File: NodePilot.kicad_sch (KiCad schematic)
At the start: 44 parts, among them K1 SRD-05VDC-SL-C, Q1 2N3904, Q2 2N2222, Q4 2N3904, T1 1:1 600R, T2 1:1 600R, U1 PC817, U2 PC817, U3 B0505S-1WR2, U4 LM358_DFN

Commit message: footprints resistors caps and diode
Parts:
- C1, C2, C3, C4, C5, C6, C8: footprint (none) -> Capacitor_THT:CP_Radial_D5.0mm_P2.50mm
- C10, C11, C7, C9: footprint (none) -> C_Disc_D5.0mm_W2.5mm_P2.50mm
- R1, R10, R11, R12, R13, R14, R16, R17, R18, R19, R2, R20, R3, R4, R5, R6, R7, R8, R9: footprint (none) -> R_Axial_DIN0204_L3.6mm_D1.6mm_P5.08mm_Horizontal
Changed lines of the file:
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@@
 			)
 		)
-		(property "Footprint" ""
+		(property "Footprint" "C_Disc_D5.0mm_W2.5mm_P2.50mm"
 			(at 95.25 88.9 0)
 			(hide yes)
@@
 			)
 		)
-		(property "Footprint" ""
+		(property "Footprint" "R_Axial_DIN0204_L3.6mm_D1.6mm_P5.08mm_Horizontal"
 			(at 49.276 71.374 90)
 			(hide yes)
@@
 			)
 		)
-		(property "Footprint" ""
+		(property "Footprint" "R_Axial_DIN0204_L3.6mm_D1.6mm_P5.08mm_Horizontal"
 			(at 122.936 48.514 90)
 			(hide yes)
@@
 			)
 		)
-		(property "Footprint" ""
+		(property "Footprint" "Capacitor_THT:CP_Radial_D5.0mm_P2.50mm"
 			(at 114.3 110.1852 0)
 			(hide yes)
@@
 			)
 		)
-		(property "Footprint" ""
+		(property "Footprint" "R_Axial_DIN0204_L3.6mm_D1.6mm_P5.08mm_Horizontal"
 			(at 106.934 70.104 90)
 			(hide yes)
@@
 			)
 		)
-		(property "Footprint" ""
+		(property "Footprint" "C_Disc_D5.0mm_W2.5mm_P2.50mm"
 			(at 110.49 119.38 0)
 			(hide yes)
@@
 			)
 		)
-		(property "Footprint" ""
+		(property "Footprint" "Capacitor_THT:CP_Radial_D5.0mm_P2.50mm"
 			(at 114.3 101.9048 0)
 			(hide yes)
@@
 			)
 		)
-		(property "Footprint" ""
+		(property "Footprint" "C_Disc_D5.0mm_W2.5mm_P2.50mm"
 			(at 184.15 92.71 0)
 			(hide yes)
@@
 			)
 		)
-		(property "Footprint" ""
+		(property "Footprint" "R_Axial_DIN0204_L3.6mm_D1.6mm_P5.08mm_Horizontal"
 			(at 211.074 82.804 90)
 			(hide yes)
@@
 			)
 		)
-		(property "Footprint" ""
+		(property "Footprint" "R_Axial_DIN0204_L3.6mm_D1.6mm_P5.08mm_Horizontal"
 			(at 86.106 180.594 90)
 			(hide yes)
@@
 			)
 		)
-		(property "Footprint" ""
+		(property "Footprint" "Capacitor_THT:CP_Radial_D5.0mm_P2.50mm"
 			(at 128.27 23.1648 0)
 			(hide yes)
@@
 			)
 		)
-		(property "Footprint" ""
+		(property "Footprint" "R_Axial_DIN0204_L3.6mm_D1.6mm_P5.08mm_Horizontal"
 			(at 159.766 91.694 90)
 			(hide yes)
@@
 			)
 		)
-		(property "Footprint" ""
+		(property "Footprint" "R_Axial_DIN0204_L3.6mm_D1.6mm_P5.08mm_Horizontal"
 			(at 95.504 53.594 90)
 			(hide yes)
@@
 			)
 		)
-		(property "Footprint" ""
+		(property "Footprint" "Capacitor_THT:CP_Radial_D5.0mm_P2.50mm"
 			(at 106.68 53.6448 0)
 			(hide yes)
@@
 			)
 		)
-		(property "Footprint" ""
+		(property "Footprint" "R_Axial_DIN0204_L3.6mm_D1.6mm_P5.08mm_Horizontal"
 			(at 70.866 85.344 90)
 			(hide yes)
@@
 			)
 		)
-		(property "Footprint" ""
+		(property "Footprint" "Capacitor_THT:CP_Radial_D5.0mm_P2.50mm"
 			(at 187.96 28.2448 0)
 			(hide yes)
@@
 			)
 		)
-		(property "Footprint" ""
+		(property "Footprint" "R_Axial_DIN0204_L3.6mm_D1.6mm_P5.08mm_Horizontal"
 			(at 92.964 129.794 90)
 			(hide yes)
@@
 			)
 		)
-		(property "Footprint" ""
+		(property "Footprint" "R_Axial_DIN0204_L3.6mm_D1.6mm_P5.08mm_Horizontal"
 			(at 184.404 113.284 90)
 			(hide yes)
@@
 			)
 		)
-		(property "Footprint" ""
+		(property "Footprint" "R_Axial_DIN0204_L3.6mm_D1.6mm_P5.08mm_Horizontal"
 			(at 152.146 29.464 90)
 			(hide yes)
@@
 			)
 		)
-		(property "Footprint" ""
+		(property "Footprint" "R_Axial_DIN0204_L3.6mm_D1.6mm_P5.08mm_Horizontal"
 			(at 86.106 165.354 90)
 			(hide yes)
@@
 			)
 		)
-		(property "Footprint" ""
+		(property "Footprint" "R_Axial_DIN0204_L3.6mm_D1.6mm_P5.08mm_Horizontal"
 			(at 196.596 92.964 90)
 			(hide yes)
@@
 			)
 		)
-		(property "Footprint" ""
+		(property "Footprint" "R_Axial_DIN0204_L3.6mm_D1.6mm_P5.08mm_Horizontal"
 			(at 78.486 176.784 90)
 			(hide yes)
@@
 			)
 		)
-		(property "Footprint" ""
+		(property "Footprint" "Capacitor_THT:CP_Radial_D5.0mm_P2.50mm"
 			(at 175.26 57.4548 0)
 			(hide yes)
@@
 			)
 		)
-		(property "Footprint" ""
+		(property "Footprint" "R_Axial_DIN0204_L3.6mm_D1.6mm_P5.08mm_Horizontal"
 			(at 196.596 76.454 90)
 			(hide yes)
@@
 			)
 		)
-		(property "Footprint" ""
+		(property "Footprint" "R_Axial_DIN0204_L3.6mm_D1.6mm_P5.08mm_Horizontal"
 			(at 49.784 129.794 90)
 			(hide yes)
@@
 			)
 		)
-		(property "Footprint" ""
+		(property "Footprint" "R_Axial_DIN0204_L3.6mm_D1.6mm_P5.08mm_Horizontal"
 			(at 157.734 146.304 90)
 			(hide yes)
@@
 			)
 		)
-		(property "Footprint" ""
+		(property "Footprint" "C_Disc_D5.0mm_W2.5mm_P2.50mm"
 			(at 58.42 133.35 0)
 			(hide yes)
@@
 			)
 		)
-		(property "Footprint" ""
+		(property "Footprint" "Capacitor_THT:CP_Radial_D5.0mm_P2.50mm"
 			(at 104.4448 85.09 0)
 			(hide yes)
@@
 			)
 		)
-		(property "Footprint" ""
+		(property "Footprint" "R_Axial_DIN0204_L3.6mm_D1.6mm_P5.08mm_Horizontal"
 			(at 71.374 169.164 90)
 			(hide yes)
@@
 			)
 		)
-		(property "Footprint" ""
+		(property "Footprint" "R_Axial_DIN0204_L3.6mm_D1.6mm_P5.08mm_Horizontal"
 			(at 127.254 139.954 90)
 			(hide yes)

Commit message: footprints t1
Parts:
- JP1: footprint (none) -> Connector:JWT_A3963_1x02_P3.96mm_Vertical
- U3: symbol B0505s:B0505S-1WR2 -> B0505S-1WR2:B0505S-1WR2
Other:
- moved on the sheet: U3
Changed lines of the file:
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@@
 			)
 		)
-		(property "Footprint" ""
+		(property "Footprint" "Connector:JWT_A3963_1x02_P3.96mm_Vertical"
 			(at 195.58 64.77 0)
 			(hide yes)
@@
 	)
 	(symbol
-		(lib_id "B0505s:B0505S-1WR2")
+		(lib_id "B0505S-1WR2:B0505S-1WR2")
 		(at 115.57 102.87 0)
 		(mirror x)

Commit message: footprints t2
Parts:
- C10, C11, C7, C9: footprint C_Disc_D5.0mm_W2.5mm_P2.50mm -> Capacitor_THT:C_Disc_D5.0mm_W2.5mm_P2.50mm
- R1, R10, R11, R12, R13, R14, R16, R17, R18, R19, R2, R20, R3, R4, R5, R6, R7, R8, R9: footprint R_Axial_DIN0204_L3.6mm_D1.6mm_P5.08mm_Horizontal -> Resistor_THT:R_Axial_DIN0204_L3.6mm_D1.6mm_P5.08mm_Horizontal
- RV1, RV2: footprint (none) -> Potentiometer_THT:Potentiometer_Bourns_3386W_Horizontal
- U3: footprint B0505S-1WR2_MNS -> B0505S-WR1:B0505S-1WR2_MNS
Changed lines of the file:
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@@
 			)
 		)
-		(property "Footprint" "C_Disc_D5.0mm_W2.5mm_P2.50mm"
+		(property "Footprint" "Capacitor_THT:C_Disc_D5.0mm_W2.5mm_P2.50mm"
 			(at 95.25 88.9 0)
 			(hide yes)
@@
 			)
 		)
-		(property "Footprint" "R_Axial_DIN0204_L3.6mm_D1.6mm_P5.08mm_Horizontal"
+		(property "Footprint" "Resistor_THT:R_Axial_DIN0204_L3.6mm_D1.6mm_P5.08mm_Horizontal"
 			(at 49.276 71.374 90)
 			(hide yes)
@@
 			)
 		)
-		(property "Footprint" "R_Axial_DIN0204_L3.6mm_D1.6mm_P5.08mm_Horizontal"
+		(property "Footprint" "Resistor_THT:R_Axial_DIN0204_L3.6mm_D1.6mm_P5.08mm_Horizontal"
 			(at 122.936 48.514 90)
 			(hide yes)
@@
 			)
 		)
-		(property "Footprint" "R_Axial_DIN0204_L3.6mm_D1.6mm_P5.08mm_Horizontal"
+		(property "Footprint" "Resistor_THT:R_Axial_DIN0204_L3.6mm_D1.6mm_P5.08mm_Horizontal"
 			(at 106.934 70.104 90)
 			(hide yes)
@@
 			)
 		)
-		(property "Footprint" "C_Disc_D5.0mm_W2.5mm_P2.50mm"
+		(property "Footprint" "Capacitor_THT:C_Disc_D5.0mm_W2.5mm_P2.50mm"
 			(at 110.49 119.38 0)
 			(hide yes)
@@
 			)
 		)
-		(property "Footprint" "C_Disc_D5.0mm_W2.5mm_P2.50mm"
+		(property "Footprint" "Capacitor_THT:C_Disc_D5.0mm_W2.5mm_P2.50mm"
 			(at 184.15 92.71 0)
 			(hide yes)
@@
 			)
 		)
-		(property "Footprint" "R_Axial_DIN0204_L3.6mm_D1.6mm_P5.08mm_Horizontal"
+		(property "Footprint" "Resistor_THT:R_Axial_DIN0204_L3.6mm_D1.6mm_P5.08mm_Horizontal"
 			(at 211.074 82.804 90)
 			(hide yes)
@@
 			)
 		)
-		(property "Footprint" "R_Axial_DIN0204_L3.6mm_D1.6mm_P5.08mm_Horizontal"
+		(property "Footprint" "Resistor_THT:R_Axial_DIN0204_L3.6mm_D1.6mm_P5.08mm_Horizontal"
 			(at 86.106 180.594 90)
 			(hide yes)
@@
 			)
 		)
-		(property "Footprint" "R_Axial_DIN0204_L3.6mm_D1.6mm_P5.08mm_Horizontal"
+		(property "Footprint" "Resistor_THT:R_Axial_DIN0204_L3.6mm_D1.6mm_P5.08mm_Horizontal"
 			(at 159.766 91.694 90)
 			(hide yes)
@@
 			)
 		)
-		(property "Footprint" ""
+		(property "Footprint" "Potentiometer_THT:Potentiometer_Bourns_3386W_Horizontal"
 			(at 170.18 29.21 0)
 			(hide yes)
@@
 			)
 		)
-		(property "Footprint" "R_Axial_DIN0204_L3.6mm_D1.6mm_P5.08mm_Horizontal"
+		(property "Footprint" "Resistor_THT:R_Axial_DIN0204_L3.6mm_D1.6mm_P5.08mm_Horizontal"
 			(at 95.504 53.594 90)
 			(hide yes)
@@
 			)
 		)
-		(property "Footprint" "R_Axial_DIN0204_L3.6mm_D1.6mm_P5.08mm_Horizontal"
+		(property "Footprint" "Resistor_THT:R_Axial_DIN0204_L3.6mm_D1.6mm_P5.08mm_Horizontal"
 			(at 70.866 85.344 90)
 			(hide yes)
@@
 			)
 		)
-		(property "Footprint" "R_Axial_DIN0204_L3.6mm_D1.6mm_P5.08mm_Horizontal"
+		(property "Footprint" "Resistor_THT:R_Axial_DIN0204_L3.6mm_D1.6mm_P5.08mm_Horizontal"
 			(at 92.964 129.794 90)
 			(hide yes)
@@
 			)
 		)
-		(property "Footprint" "R_Axial_DIN0204_L3.6mm_D1.6mm_P5.08mm_Horizontal"
+		(property "Footprint" "Resistor_THT:R_Axial_DIN0204_L3.6mm_D1.6mm_P5.08mm_Horizontal"
 			(at 184.404 113.284 90)
 			(hide yes)
@@
 			)
 		)
-		(property "Footprint" "R_Axial_DIN0204_L3.6mm_D1.6mm_P5.08mm_Horizontal"
+		(property "Footprint" "Resistor_THT:R_Axial_DIN0204_L3.6mm_D1.6mm_P5.08mm_Horizontal"
 			(at 152.146 29.464 90)
 			(hide yes)
@@
 			)
 		)
-		(property "Footprint" "R_Axial_DIN0204_L3.6mm_D1.6mm_P5.08mm_Horizontal"
+		(property "Footprint" "Resistor_THT:R_Axial_DIN0204_L3.6mm_D1.6mm_P5.08mm_Horizontal"
 			(at 86.106 165.354 90)
 			(hide yes)
@@
 			)
 		)
-		(property "Footprint" "R_Axial_DIN0204_L3.6mm_D1.6mm_P5.08mm_Horizontal"
+		(property "Footprint" "Resistor_THT:R_Axial_DIN0204_L3.6mm_D1.6mm_P5.08mm_Horizontal"
 			(at 196.596 92.964 90)
 			(hide yes)
@@
 			)
 		)
-		(property "Footprint" ""
+		(property "Footprint" "Potentiometer_THT:Potentiometer_Bourns_3386W_Horizontal"
 			(at 162.56 54.61 0)
 			(hide yes)
@@
 			)
 		)
-		(property "Footprint" "R_Axial_DIN0204_L3.6mm_D1.6mm_P5.08mm_Horizontal"
+		(property "Footprint" "Resistor_THT:R_Axial_DIN0204_L3.6mm_D1.6mm_P5.08mm_Horizontal"
 			(at 78.486 176.784 90)
 			(hide yes)
@@
 			)
 		)
-		(property "Footprint" "R_Axial_DIN0204_L3.6mm_D1.6mm_P5.08mm_Horizontal"
+		(property "Footprint" "Resistor_THT:R_Axial_DIN0204_L3.6mm_D1.6mm_P5.08mm_Horizontal"
 			(at 196.596 76.454 90)
 			(hide yes)
@@
 			)
 		)
-		(property "Footprint" "B0505S-1WR2_MNS"
+		(property "Footprint" "B0505S-WR1:B0505S-1WR2_MNS"
 			(at 115.57 102.87 0)
 			(hide yes)
@@
 			)
 		)
-		(property "Footprint" "R_Axial_DIN0204_L3.6mm_D1.6mm_P5.08mm_Horizontal"
+		(property "Footprint" "Resistor_THT:R_Axial_DIN0204_L3.6mm_D1.6mm_P5.08mm_Horizontal"
 			(at 49.784 129.794 90)
 			(hide yes)
@@
 			)
 		)
-		(property "Footprint" "R_Axial_DIN0204_L3.6mm_D1.6mm_P5.08mm_Horizontal"
+		(property "Footprint" "Resistor_THT:R_Axial_DIN0204_L3.6mm_D1.6mm_P5.08mm_Horizontal"
 			(at 157.734 146.304 90)
 			(hide yes)
@@
 			)
 		)
-		(property "Footprint" "C_Disc_D5.0mm_W2.5mm_P2.50mm"
+		(property "Footprint" "Capacitor_THT:C_Disc_D5.0mm_W2.5mm_P2.50mm"
 			(at 58.42 133.35 0)
 			(hide yes)
@@
 			)
 		)
-		(property "Footprint" "R_Axial_DIN0204_L3.6mm_D1.6mm_P5.08mm_Horizontal"
+		(property "Footprint" "Resistor_THT:R_Axial_DIN0204_L3.6mm_D1.6mm_P5.08mm_Horizontal"
 			(at 71.374 169.164 90)
 			(hide yes)
@@
 			)
 		)
-		(property "Footprint" "R_Axial_DIN0204_L3.6mm_D1.6mm_P5.08mm_Horizontal"
+		(property "Footprint" "Resistor_THT:R_Axial_DIN0204_L3.6mm_D1.6mm_P5.08mm_Horizontal"
 			(at 127.254 139.954 90)
 			(hide yes)

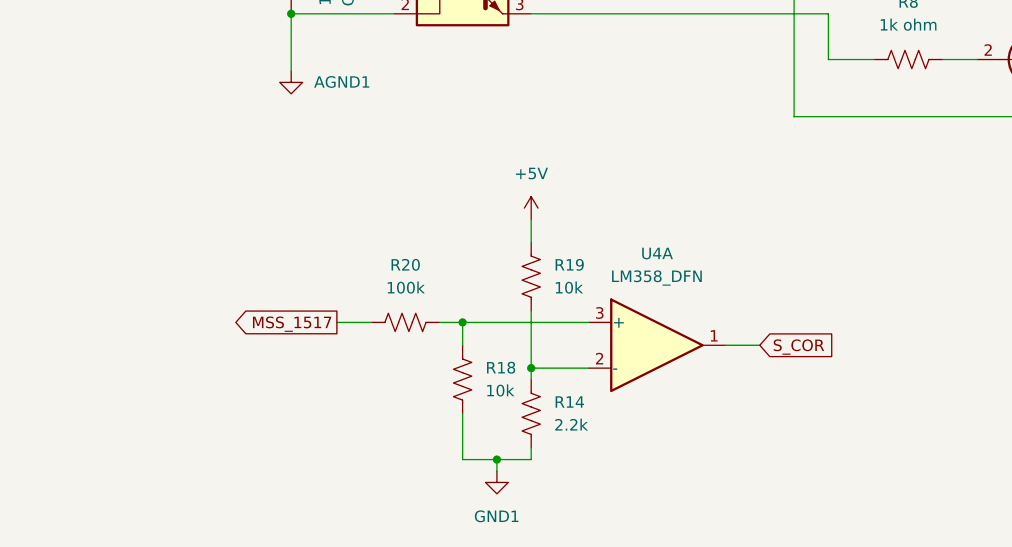
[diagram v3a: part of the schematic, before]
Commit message: proper designators
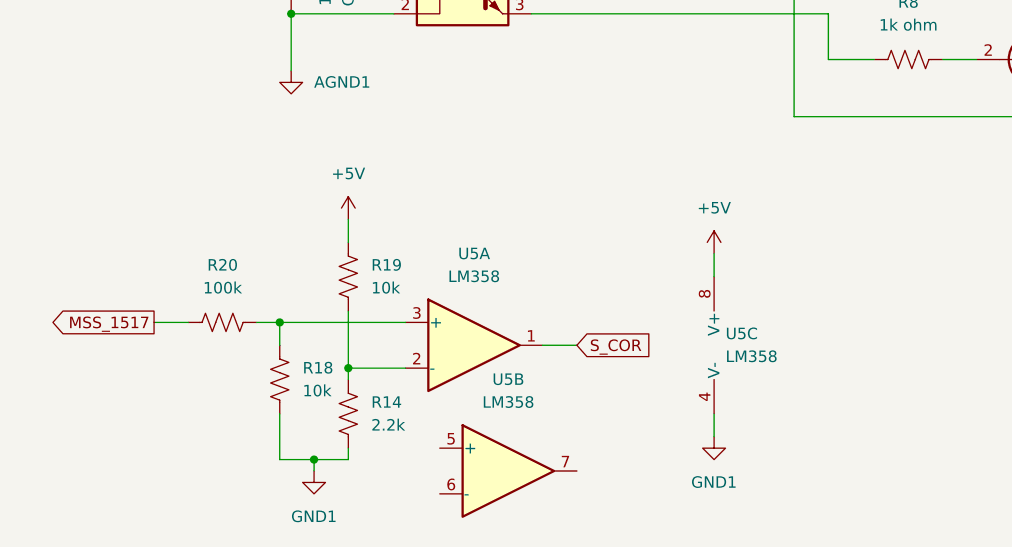
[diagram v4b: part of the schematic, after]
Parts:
- removed U4: LM358_DFN, Package_DFN_QFN:DFN-8-1EP_2x2mm_P0.5mm_EP1.05x1.75mm, symbol Amplifier_Operational:LM358_DFN
- added U5: LM358, symbol Amplifier_Operational:LM358
- R14, R18, R19, R20: footprint Resistor_THT:R_Axial_DIN0204_L3.6mm_D1.6mm_P5.08mm_Horizontal -> (none)
- T1, T2: footprint (none) -> Transformer_THT:Transformer_Toroid_Horizontal_D10.5mm_Amidon-T37
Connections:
- net +5V: now also U5.8 (V+)
- net GND1: now also U5.4 (V-)
- net S_COR: now also U5.1
- net at R14.1, R19.2: now also U5.2 (-)
- net at R18.1, R20.2: now also U5.3 (+)
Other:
- moved on the sheet: R14, R18, R19, R20

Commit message: proper designator
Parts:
- JP1: footprint Connector:JWT_A3963_1x02_P3.96mm_Vertical -> TerminalBlock_Phoenix:TerminalBlock_Phoenix_PT-1,5-2-3.5-H_1x02_P3.50mm_Horizontal
- RV1, RV2: footprint Potentiometer_THT:Potentiometer_Bourns_3386W_Horizontal -> Potentiometer_THT:Potentiometer_Bourns_3296W_Vertical
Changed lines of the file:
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@@
 			)
 		)
-		(property "Footprint" "Connector:JWT_A3963_1x02_P3.96mm_Vertical"
+		(property "Footprint" "TerminalBlock_Phoenix:TerminalBlock_Phoenix_PT-1,5-2-3.5-H_1x02_P3.50mm_Horizontal"
 			(at 195.58 64.77 0)
 			(hide yes)
@@
 			)
 		)
-		(property "Footprint" "Potentiometer_THT:Potentiometer_Bourns_3386W_Horizontal"
+		(property "Footprint" "Potentiometer_THT:Potentiometer_Bourns_3296W_Vertical"
 			(at 170.18 29.21 0)
 			(hide yes)
@@
 			)
 		)
-		(property "Footprint" "Potentiometer_THT:Potentiometer_Bourns_3386W_Horizontal"
+		(property "Footprint" "Potentiometer_THT:Potentiometer_Bourns_3296W_Vertical"
 			(at 162.56 54.61 0)
 			(hide yes)

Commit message: proper footprint
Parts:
- removed T1, T2: 1:1 600R, Transformer_THT:Transformer_Toroid_Horizontal_D10.5mm_Amidon-T37, symbol Device:Transformer_1P_1S_SO8
- added T1, T2: 1:1 600R, Diode_THT:Diode_Bridge_DIP-4_W7.62mm_P5.08mm, symbol Device:Transformer_1P_1S
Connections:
- net AGND1: now also T1.1 (AA), T2.2 (AB)
- net RIGGND: now also T2.3 (SA)
- net at C1.1, R9.2: now also T1.2 (AB)
- net at C11.2, K1.4, Q1.1 (E)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: now also T1.4 (SB)
- net at C2.2: now also T2.1 (AA)
- net at RV2.2: now also T1.3 (SA)
- net at R6.1, RV1.3: now also T2.4 (SB)
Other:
- moved on the sheet: R6

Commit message: super update
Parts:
- added R15: 0 ohm, Resistor_THT:R_Axial_DIN0204_L3.6mm_D1.6mm_P5.08mm_Horizontal, symbol Device:R_US
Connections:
- net AGND1: now also R15.1; no longer C10.1, U1.2
- new net: C10.1, R15.2, U1.2
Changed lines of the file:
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@@
 	)
 	(junction
+		(at 58.42 135.89)
+		(diameter 0)
+		(color 0 0 0 0)
+	)
+	(junction
 		(at 121.92 54.61)
 		(diameter 0)
@@
 	)
 	(junction
-		(at 58.42 135.89)
-		(diameter 0)
-		(color 0 0 0 0)
-	)
-	(junction
 		(at 60.96 185.42)
 		(diameter 0)
@@
 	(wire
 		(pts
+			(xy 58.42 137.16) (xy 58.42 135.89)
+		)
+		(stroke
+			(width 0)
+			(type default)
+		)
+	)
+	(wire
+		(pts
 			(xy 104.14 119.38) (xy 104.14 130.81)
 		)
@@
 	(wire
 		(pts
+			(xy 58.42 144.78) (xy 58.42 146.05)
+		)
+		(stroke
+			(width 0)
+			(type default)
+		)
+	)
+	(wire
+		(pts
 			(xy 85.09 130.81) (xy 88.9 130.81)
 		)
@@
 	(wire
 		(pts
-			(xy 58.42 135.89) (xy 58.42 142.24)
-		)
-		(stroke
-			(width 0)
-			(type default)
-		)
-	)
-	(wire
-		(pts
 			(xy 114.3 109.22) (xy 114.3 119.38)
 		)
@@
 	(symbol
 		(lib_id "power:GND1")
-		(at 58.42 142.24 0)
+		(at 58.42 146.05 0)
 		(unit 1)
 		(body_style 1)
@@
 		(fields_autoplaced yes)
 		(property "Reference" "#PWR05"
-			(at 58.42 148.59 0)
+			(at 58.42 152.4 0)
 			(hide yes)
 			(show_name no)
@@
 		)
 		(property "Value" "AGND1"
-			(at 60.96 143.5099 0)
+			(at 60.96 147.3199 0)
 			(show_name no)
 			(do_not_autoplace no)
@@
 		)
 		(property "Footprint" ""
-			(at 58.42 142.24 0)
+			(at 58.42 146.05 0)
 			(hide yes)
 			(show_name no)
@@
 		)
 		(property "Datasheet" ""
-			(at 58.42 142.24 0)
+			(at 58.42 146.05 0)
 			(hide yes)
 			(show_name no)
@@
 		)
 		(property "Description" "Power symbol creates a global label with name \"GND1\" , ground"
-			(at 58.42 142.24 0)
+			(at 58.42 146.05 0)
 			(hide yes)
 			(show_name no)
@@
 					(unit 1)
 				)
+			)
+		)
+	)
+	(symbol
+		(lib_id "Device:R_US")
+		(at 58.42 140.97 180)
+		(unit 1)
+		(body_style 1)
+		(exclude_from_sim no)
+		(in_bom yes)
+		(on_board yes)
+		(in_pos_files yes)
+		(dnp no)
+		(property "Reference" "R15"
+			(at 52.07 140.97 90)
+			(show_name no)
+			(do_not_autoplace no)
+			(effects
+				(font
+					(size 1.27 1.27)
+				)
+			)
+		)
+		(property "Value" "0 ohm"
+			(at 54.61 140.97 90)
+			(show_name no)
+			(do_not_autoplace no)
+			(effects
+				(font
+					(size 1.27 1.27)
+				)
+			)
+		)
+		(property "Footprint" "Resistor_THT:R_Axial_DIN0204_L3.6mm_D1.6mm_P5.08mm_Horizontal"
+			(at 57.404 140.716 90)
+			(hide yes)
+			(show_name no)
+			(do_not_autoplace no)
+			(effects
+				(font
+					(size 1.27 1.27)
+				)
+			)
+		)
+		(property "Datasheet" ""
+			(at 58.42 140.97 0)
+			(hide yes)
+			(show_name no)
+			(do_not_autoplace no)
+			(effects
+				(font
+					(size 1.27 1.27)
+				)
+			)
+		)
+		(property "Description" "Resistor, US symbol"
+			(at 58.42 140.97 0)
+			(hide yes)
+			(show_name no)
+			(do_not_autoplace no)
+			(effects
+				(font
+					(size 1.27 1.27)
+				)
+			)
+		)
+		(pin "1"
+		)
+		(pin "2"
+		)
+		(instances
+			(project "NodePilot"
+				(path "/feb6dcc4-ba57-4640-ad64-1efd302ce012"
+					(reference "R15")
+					(unit 1)
+				)
